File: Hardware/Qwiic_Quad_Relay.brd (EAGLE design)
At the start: 82.5 x 47 mm, 122 parts, among them J2 Qwiic Right Angle, J3 Qwiic Right Angle, J4 AVR_SPI_PROG_3X2TESTPOINTS, J9 POWER_JACK, K1 RELAY-SPDT-JZC-11F, K2 RELAY-SPDT-JZC-11F, K3 RELAY-SPDT-JZC-11F, K4 RELAY-SPDT-JZC-11F, Q1 600mA/40V, Q2 600mA/40V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

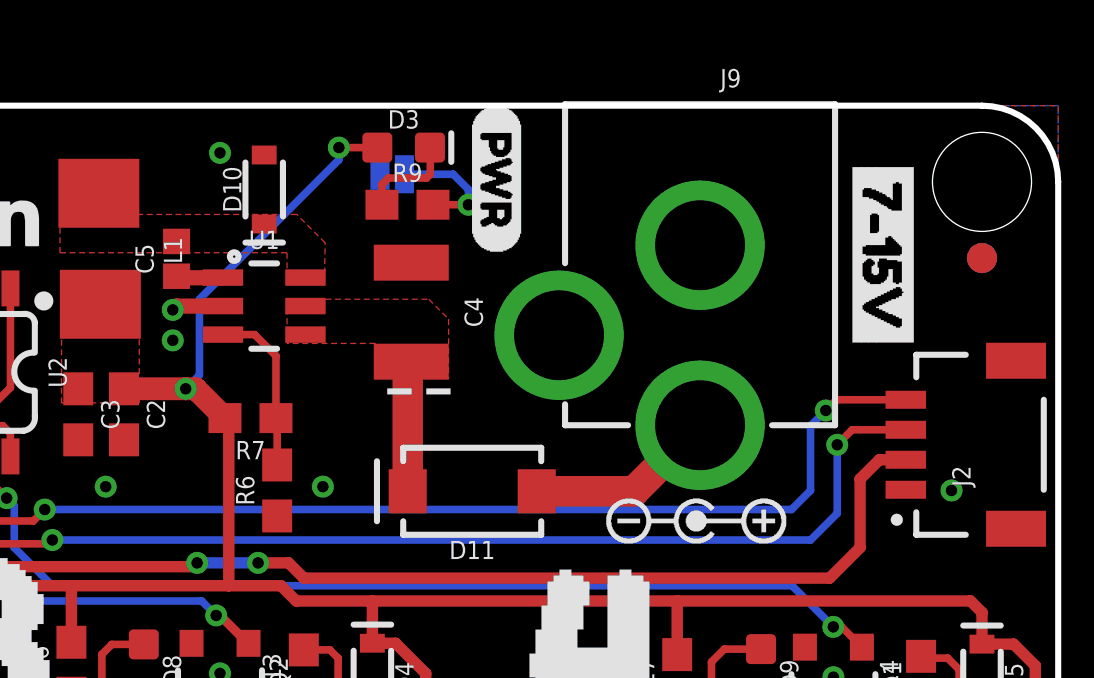
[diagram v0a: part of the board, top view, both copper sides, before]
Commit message: Adjusts silk, add bypass jumper, corrects feedback pin resistor values -> output: 5.35V
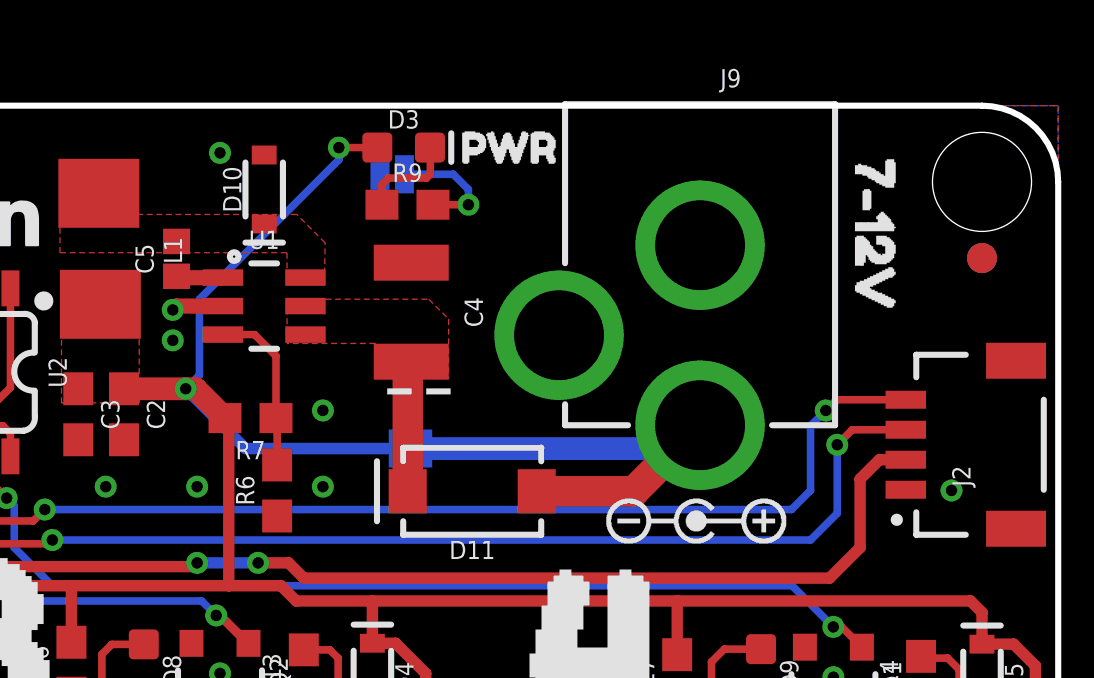
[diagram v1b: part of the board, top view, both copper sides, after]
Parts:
- removed U$53: (no value), 7-15V:7#15V0
- added BYP: JUMPER-SMT_2_NO_SILK, SparkFun-Jumpers:SMT-JUMPER_2_NO_SILK
- added U$14: (no value), SparkFun-Buzzard:BYP
- added U$46: (no value), SparkFun-Buzzard:PWR_TO
- R6: value 20k -> 2.0k
- R7: value 100k -> 12k
- U$1: device Labels:PWR-()-04 -> POWER_IN:7#12V0
- U$49: device 7-15V:7#15V0 -> POWER_IN:7#12V0
- moved U$1 12.6 mm to (76.5, 46.4)
- moved U$52 1.20 mm to (64.4, 32.5)
- moved U$50 1.09 mm to (67.4, 33.8)
- moved U$49 0.77 mm to (76.6, 46.4), flipped to the bottom
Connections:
- net 5V: now also BYP.2
- net VIN: now also BYP.1
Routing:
- net VIN: track 6.36 -> 15.9 mm
- net 5V: track 172.5 -> 180.4 mm
- net GND: vias 19 -> 21

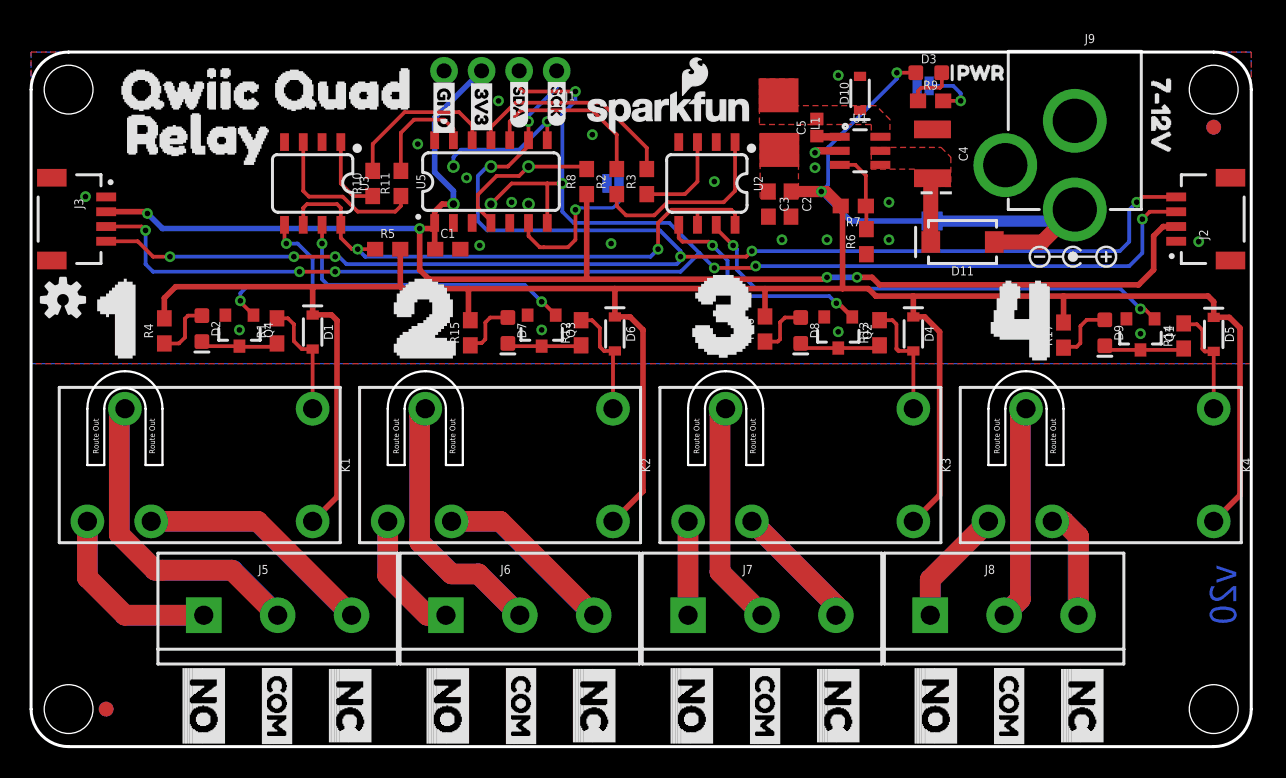
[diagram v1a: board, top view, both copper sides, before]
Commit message: Updates schematic
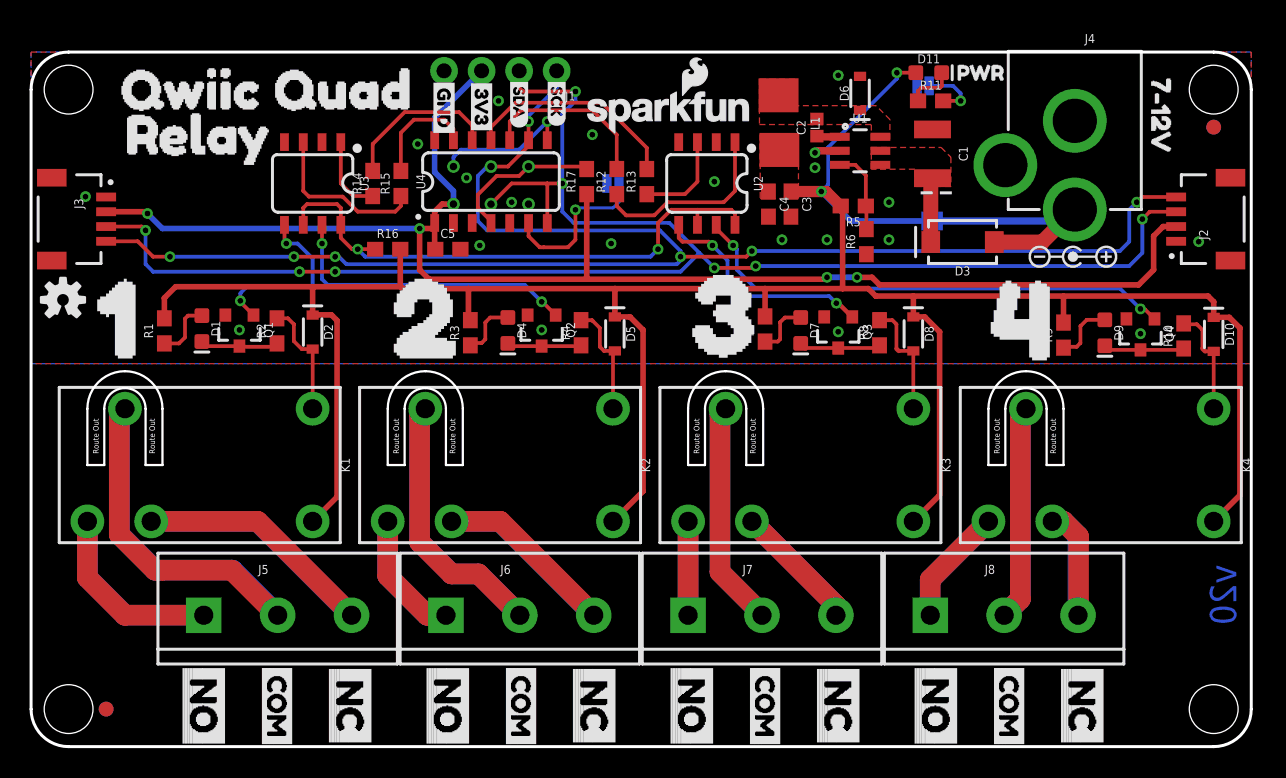
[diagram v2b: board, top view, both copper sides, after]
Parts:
- removed ADDR, BYP, LED: JUMPER-SMT_2_NO_SILK, SparkFun-Jumpers:SMT-JUMPER_2_NO_SILK
- removed JP8, JP9: FIDUCIAL1X2, SparkFun-Aesthetics:FIDUCIAL-1X2
- added FD1, FD2, FD3, FD4: FIDUCIAL1X2, SparkFun-Aesthetics:FIDUCIAL-1X2
- added JP7: STAND-OFF, SparkFun:STAND-OFF
- C1: value 0.1uF -> 10uF; device SparkFun-Capacitors:0603 -> SparkFun-Capacitors:EIA3528
- C2: value 10uF -> 0.1uF; device SparkFun-Capacitors:0603 -> SparkFun-Capacitors:0402
- C4: device SparkFun-Capacitors:EIA3528 -> SparkFun-Capacitors:0603
- C5: device SparkFun-Capacitors:0402 -> SparkFun-Capacitors:0603
- D1, D4: value 1A/23V/620mV -> BLUE; device SparkFun-DiscreteSemi:SOD-323 -> SparkFun-LED:LED-0603
- D10: value 3A/10V/280mV -> 1A/23V/620mV
- D11: value 1A/40V/500mV -> RED; device SparkFun-DiscreteSemi:SMA-DIODE -> SparkFun-LED:LED-0603
- D2, D8: value BLUE -> 1A/23V/620mV; device SparkFun-LED:LED-0603 -> SparkFun-DiscreteSemi:SOD-323
- D3: value RED -> 1A/40V/500mV; device SparkFun-LED:LED-0603 -> SparkFun-DiscreteSemi:SMA-DIODE
- D6: value 1A/23V/620mV -> 3A/10V/280mV
- J4: value AVR_SPI_PROG_3X2TESTPOINTS -> POWER_JACK; device SparkFun-Connectors:2X3_TEST_POINTS -> SparkFun-Connectors:POWER_JACK_PTH
- J9: value POWER_JACK -> AVR_SPI_PROG_3X2TESTPOINTS; device SparkFun-Connectors:POWER_JACK_PTH -> SparkFun-Connectors:2X3_TEST_POINTS
- JP1, JP3: value STAND-OFF -> JUMPER-SMT_2_NO_SILK; device SparkFun:STAND-OFF -> SparkFun-Jumpers:SMT-JUMPER_2_NO_SILK
- JP2: value FIDUCIAL1X2 -> JUMPER-SMT_2_NO_SILK; device SparkFun-Aesthetics:FIDUCIAL-1X2 -> SparkFun-Jumpers:SMT-JUMPER_2_NO_SILK
- JP6: value FIDUCIAL1X2 -> STAND-OFF; device SparkFun-Aesthetics:FIDUCIAL-1X2 -> SparkFun:STAND-OFF
- LOGO1: value OSHW-LOGOS -> SFE_LOGO_NAME_FLAME.1_INCH; device SparkFun-Aesthetics:OSHW-LOGO-S -> SparkFun-Aesthetics:SFE_LOGO_NAME_FLAME_.1
- LOGO2: value SFE_LOGO_NAME_FLAME.1_INCH -> OSHW-LOGOS; device SparkFun-Aesthetics:SFE_LOGO_NAME_FLAME_.1 -> SparkFun-Aesthetics:OSHW-LOGO-S
- R1: value 33 -> 1k
- R10, R2: value 100 -> 33
- R11, R3: value 100 -> 1k
- R12, R13, R14: value 33 -> 100
- R15: value 1k -> 100
- R16: value 1k -> 330
- R17: value 1k -> 10k
- R4: value 1k -> 33
- R5: value 330 -> 12k
- R7: value 12k -> 1k
- R8: value 10k -> 33
- moved JP4 77.5 mm to (2.54, 44.5)
- moved JP1 67.1 mm to (61.0, 35.6), flipped to the bottom
- moved Q1 61.0 mm to (14.1, 28.2)
- moved Q4 61.0 mm to (75.1, 27.9)
- moved R10 55.8 mm to (78.0, 27.8)
- moved R14 55.8 mm to (23.1, 38.1)
- moved LOGO1 42.9 mm to (43.2, 42.9)
- moved LOGO2 42.9 mm to (2.16, 30.2)
- moved JP5 41.9 mm to (80.0, 44.5)
- moved J4 41.3 mm to (70.6, 50.0), flipped to the top
- moved J9 41.3 mm to (31.1, 38.0), flipped to the bottom
- moved D5 40.5 mm to (39.5, 27.9)
- moved JP3 37.4 mm to (39.4, 38.1), flipped to the bottom
- moved R11 36.3 mm to (60.9, 43.7), turned to 0 degrees
- moved R17 33.9 mm to (37.6, 38.2)
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- renumbered FRAME2 to FRAME1, U5 to U4
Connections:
- net !RESET: now also J9.5, R17.2; no longer J4.5, R8.2
- net 3.3V: now also C5.1, J9.2, R17.1; no longer C1.1, J4.2, R8.1
- net 5V: now also C4.1, D10.C, D11.A, D2.C, D8.C, JP1.2, R1.2, R3.2, R9.2; no longer BYP.2, C2.1, D1.C, D3.A, D4.C, D6.C, R15.2, R17.2, R4.2
- net ADDR_JUMP: now also JP3.1; no longer ADDR.1
- net CB: now also C2.1; no longer C5.1
- net FB: now also R5.1; no longer R7.1
- net GND: now also C1.C, C4.2, C5.2, D6.A, J4.GND, J4.GNDBREAK, J9.6, JP2.1, JP3.2; no longer ADDR.2, C1.2, C2.2, C4.C, D10.A, J4.6, J9.GND, J9.GNDBREAK, LED.1
- net MISO: now also J9.1; no longer J4.1
- net N$1: now also D1.A, R1.1; no longer D2.A, R4.1
- net N$10: now also D2.A, R2.2; no longer D1.A, R1.2
- net N$11: now also R13.1; no longer R3.1
- net N$12: now also D4.C, Q2.3, R4.1; no longer D7.C, Q3.3, R12.1
- net N$13: now also D11.C, R11.1; no longer D3.C, R9.1
- net N$14: now also JP2.2, R11.2; no longer LED.2, R9.2
- net N$15: now also D7.C, Q3.3, R8.1; no longer D8.C, Q2.3, R13.1
- net N$17: now also Q4.3, R10.1; no longer Q1.3, R14.1
- net N$18: now also D5.A, R4.2; no longer D6.A, R12.2
- net N$2: now also D1.C, Q1.3, R2.1; no longer D2.C, Q4.3, R1.1
- net N$23: now also D8.A, R8.2; no longer D4.A, R13.2
- net N$24: now also D10.A, R10.2; no longer D5.A, R14.2
- net N$3: now also R15.1; no longer R11.1
- net N$4: now also D4.A, R3.1; no longer D7.A, R15.1
- net N$5: now also R14.1; no longer R10.1
- net N$6: now also R16.1; no longer R5.1
- net N$7: now also D7.A, R7.1; no longer D8.A, R16.1
- net N$8: now also R9.1; no longer R17.1
- net N$9: now also R12.1; no longer R2.1
- net OPTO_1: now also Q1.1; no longer Q4.1
- net OPTO_2: now also Q2.1; no longer Q3.1
- net OPTO_3: now also Q3.1; no longer Q2.1
- net OPTO_4: now also Q4.1; no longer Q1.1
- net RELAY_CTRL1: now also R12.2; no longer R2.2
- net RELAY_CTRL2: now also R13.2; no longer R3.2
- net RELAY_CTRL3: now also R14.2; no longer R10.2
- net RELAY_CTRL4: now also R15.2; no longer R11.2
- net SCL/SCK: now also J9.3; no longer J4.3
- net SDA/MOSI: now also J9.4; no longer J4.4
- net SW: now also C2.2, D6.C; no longer C5.2, D10.C
- net VIN: now also D3.A, J4.PWR, JP1.1; no longer BYP.1, D11.A, J9.PWR
- net VIN_DC_DC: now also C1.A, D3.C; no longer C4.A, D11.C

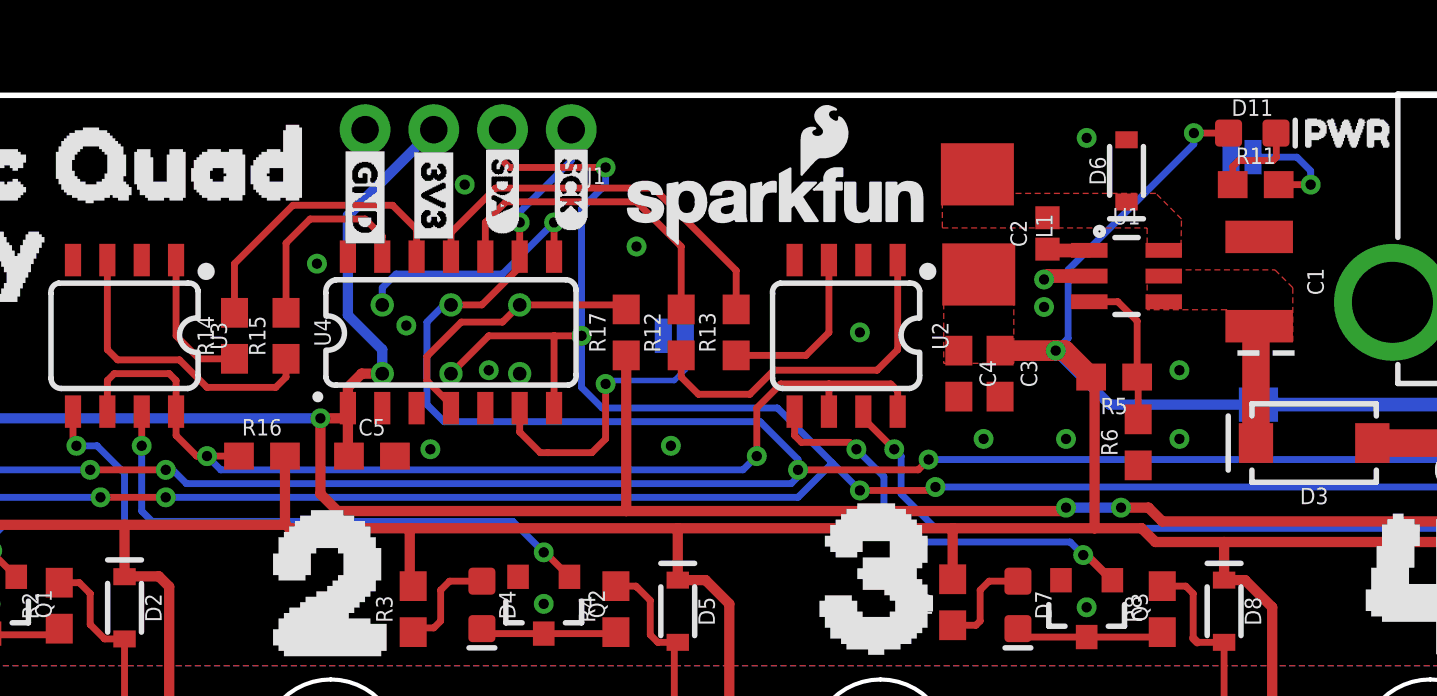
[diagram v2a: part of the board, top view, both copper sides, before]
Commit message: Adds correct inductor
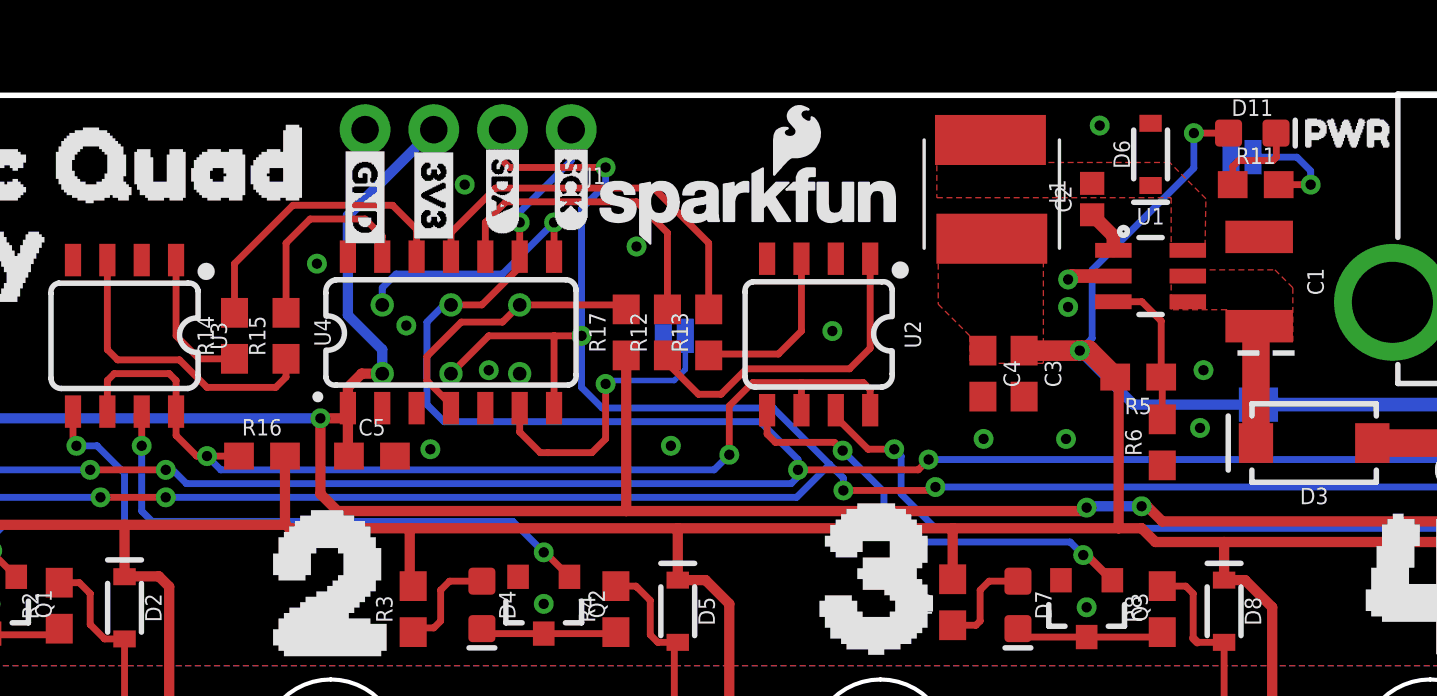
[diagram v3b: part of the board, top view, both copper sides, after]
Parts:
- added U$53: (no value), SparkFun-Buzzard:LED_32
- moved C2 2.08 mm to (54.8, 43.2)
- moved L1 1.36 mm to (51.1, 43.4)
- moved D6 1.08 mm to (57.0, 44.8)
- moved U2 1.02 mm to (44.7, 38.2)
- moved LOGO1 1.02 mm to (42.2, 42.9)
- moved LOGO3 1.02 mm to (42.2, 42.9)
- moved R13 1.02 mm to (40.6, 38.2)
- moved C3 0.89 mm to (52.3, 36.7)
- moved C4 0.89 mm to (50.8, 36.7)
- moved R5 0.89 mm to (56.5, 36.6)
- moved R6 0.89 mm to (57.4, 34.2)
- moved U1 0.89 mm to (57.0, 40.3)
- moved R12 0.51 mm to (39.1, 38.2)
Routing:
- net 5V: track 180.4 -> 179.1 mm
- net N$6: track 38.6 -> 37.6 mm
- net OPTO_4: track 33.3 -> 34.3 mm
- net N$9: track 13.1 -> 12.3 mm
- net OPTO_3: track 15.6 -> 16.3 mm

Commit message: Changes standoff to the one used in the SparkFun libraries
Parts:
- JP4, JP5, JP6, JP7: device SparkFun:STAND-OFF -> SparkFun-Hardware:STAND-OFF
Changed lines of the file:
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@@
 <attribute name="VALUE" value="330" x="24.13" y="32.893" size="0.6096" layer="27" font="vector" ratio="20" align="top-center"/>
 </element>
-<element name="JP4" library="SparkFun" package="STAND-OFF" value="STAND-OFF" x="2.54" y="44.45" smashed="yes"/>
-<element name="JP5" library="SparkFun" package="STAND-OFF" value="STAND-OFF" x="80.01" y="44.45" smashed="yes"/>
+<element name="JP4" library="SparkFun-Hardware" package="STAND-OFF" value="STAND-OFF" x="2.54" y="44.45" smashed="yes"/>
+<element name="JP5" library="SparkFun-Hardware" package="STAND-OFF" value="STAND-OFF" x="80.01" y="44.45" smashed="yes"/>
 <element name="FD1" library="SparkFun-Aesthetics" package="FIDUCIAL-1X2" value="FIDUCIAL1X2" x="80.01" y="41.91" smashed="yes" rot="MR0"/>
 <element name="FD3" library="SparkFun-Aesthetics" package="FIDUCIAL-1X2" value="FIDUCIAL1X2" x="5.08" y="2.54" smashed="yes" rot="MR0"/>
@@
 <attribute name="VALUE" x="12.446" y="28.194" size="0.6096" layer="27" font="vector" ratio="20" rot="R270" align="top-center"/>
 </element>
-<element name="JP6" library="SparkFun" package="STAND-OFF" value="STAND-OFF" x="2.54" y="2.54" smashed="yes"/>
-<element name="JP7" library="SparkFun" package="STAND-OFF" value="STAND-OFF" x="80.01" y="2.54" smashed="yes"/>
+<element name="JP6" library="SparkFun-Hardware" package="STAND-OFF" value="STAND-OFF" x="2.54" y="2.54" smashed="yes"/>
+<element name="JP7" library="SparkFun-Hardware" package="STAND-OFF" value="STAND-OFF" x="80.01" y="2.54" smashed="yes"/>
 <element name="J5" library="SparkFun-Connectors" package="SCREWTERMINAL-5MM-3" value="" x="11.684" y="8.89" smashed="yes">
 <attribute name="NAME" x="15.367" y="11.684" size="0.6096" layer="25" font="vector" ratio="20"/>
